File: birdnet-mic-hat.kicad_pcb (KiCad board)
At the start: 4 copper layers, 17.8 x 22.7 mm, 26 parts, among them J1 PJ-327A0-SMT, J3 DF40HC(3.5)-30DS-0.4V(51), Q1 MMBT3904, U1 TLV320ADC5140, U2 TPS7A2033PDBVR

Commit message: Apply 2026-10-18 design-review fixes before relayout
Schematic: R3 becomes a 100k SHDNZ pull-down; add 4.7k I2C pull-ups
(R9/R10), a 33R PDM_CLK series resistor (R11), and ESD9B5.0ST5G TVS
diodes on JACK_TIP/JACK_RING (D1/D2). C11 footprint unchanged (0603).

PCB: R11 at U1 pin 11, pull-ups and TVS diodes placed and routed;
direct top-copper ground bar from U1 AVSS (pin 4) to the VREF/MICBIAS/
AREG caps; C9 moved beside U2; U1 EPAD paste removed (vias to be
plugged at fab); ENIG finish; edge via moved inboard; new references
hidden.

Checkpoint only: C11 is parked off-board and its MIC_RING_N connection
is unrouted. This state precedes a full relayout.

Co-Authored-By: Claude Opus 5.5 <noreply@anthropic.com>
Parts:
- added D1: ESD9B5.0ST5G, Diode_SMD:D_SOD-923, F.Cu at (117.0, 116.8)
- added D2: ESD9B5.0ST5G, Diode_SMD:D_SOD-923, F.Cu at (103.2, 107.9)
- added R10: 4.7k, Resistor_SMD:R_0402_1005Metric, F.Cu at (105.4, 128.3)
- added R11: 33, Resistor_SMD:R_0402_1005Metric, F.Cu at (107.6, 118.7)
- added R9: 4.7k, Resistor_SMD:R_0402_1005Metric, F.Cu at (106.5, 128.3)
- R3: value 10k -> 100k
- moved C11 14.5 mm to (122.0, 118.0)
- moved C9 1.90 mm to (115.3, 123.8), turned to 180 degrees
- moved C4 0.60 mm to (113.4, 122.4)
- moved C1 0.58 mm to (113.4, 123.4)
- moved C5 0.50 mm to (113.4, 121.3)
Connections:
- R3 pad 1: VCC_3V3 -> GND
- U1 pad 11: /PDM_CLK -> Net-(U1-IN3M_GPO3)
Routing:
- net GND: track 22.3 -> 25.9 mm, vias 16 -> 18
- net /PDM_CLK: track 17.1 -> 14.2 mm
- net /JACK_RING: track 12.6 -> 15.2 mm
- net Net-(U1-IN3M_GPO3): track 0.00 -> 2.00 mm
- net AVDD: track 32.5 -> 34.2 mm
- net /MIC_RING_N: track 7.28 -> 8.72 mm
- net /JACK_BIAS_SENSE: track 40.0 -> 38.8 mm
- net /I2C_SCL: track 9.19 -> 10.1 mm, vias 1 -> 2
- net /I2C_SDA: track 11.7 -> 12.5 mm, vias 1 -> 2
- net /JACK_TIP: track 11.2 -> 11.9 mm

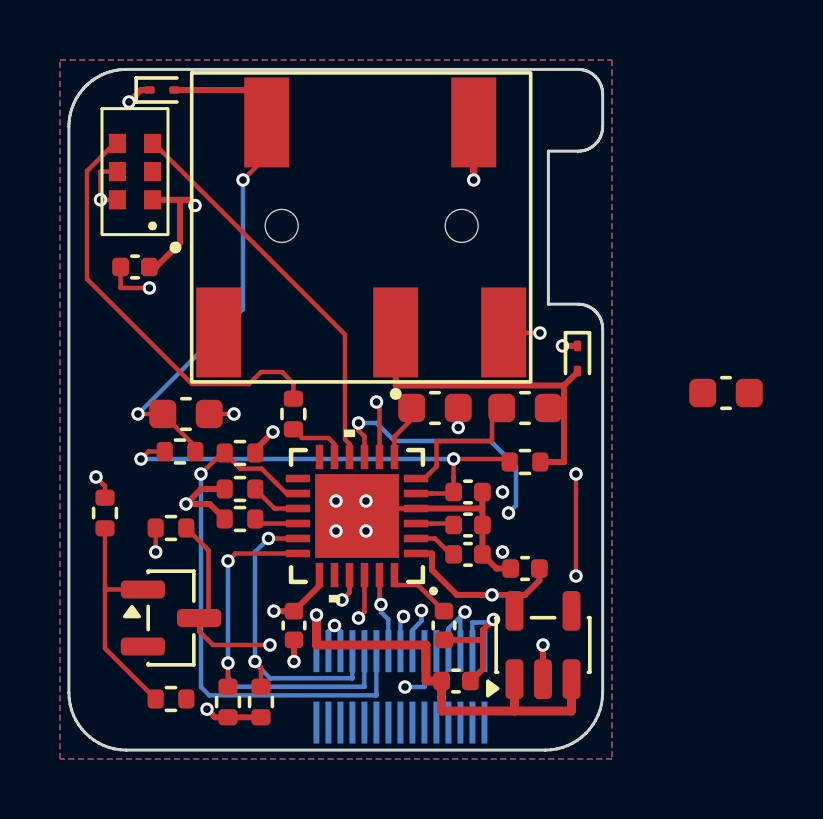
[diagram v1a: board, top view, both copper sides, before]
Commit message: Relayout: route board, swap J3 I2S/I2C GPIO assignment
Full re-route of the 2026-10-18 relayout. J3 signals were permuted so
I2S drops straight down from U1 pins 21-23: 8 SDOUT/GPIO42,
10 BCLK/GPIO41, 12 WS/GPIO40, 14 SCL/GPIO39, 16 SDA/GPIO38,
18 ADC_RST/GPIO47, 20 MIC_PRESENT/GPIO48. Firmware must follow.

U1 pad 4 zone connection set to solid (hard-wired AVSS bar).
DRC: 0 errors, 0 unconnected, parity 0; 2 known U1/J3 library
mismatch warnings. ERC: 0/0.

Co-Authored-By: Claude Opus 5.5 <noreply@anthropic.com>
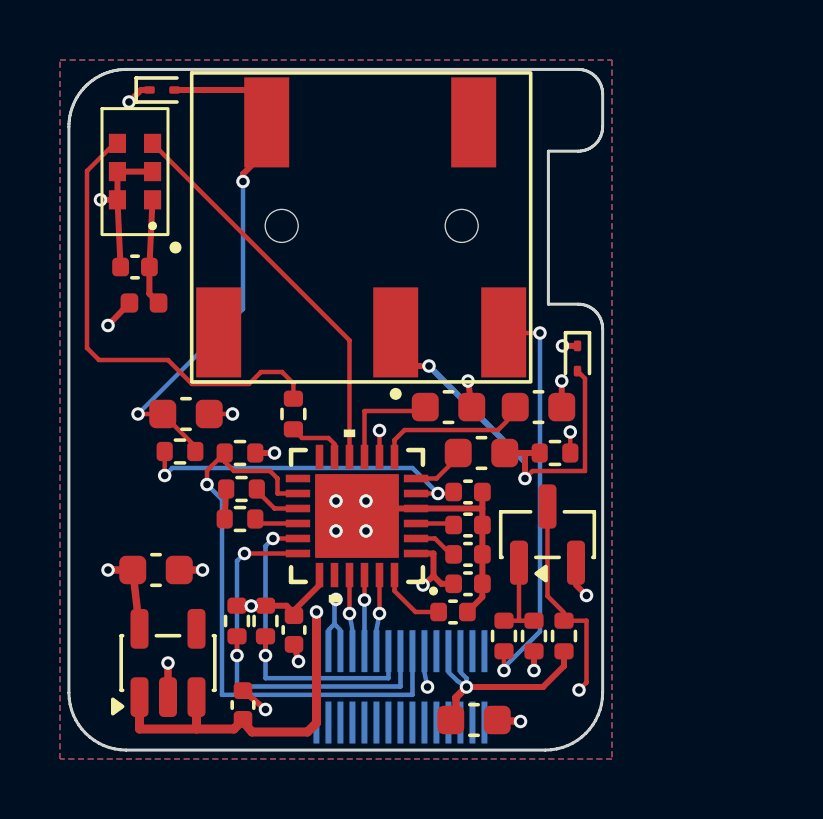
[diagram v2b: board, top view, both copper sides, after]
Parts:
- added C13: 10uF, Capacitor_SMD:C_0603_1608Metric, F.Cu at (103.0, 123.9)
- added C14: 10uF, Capacitor_SMD:C_0603_1608Metric, F.Cu at (113.6, 128.9)
- added FB1: 600R@100MHz, Inductor_SMD:L_0402_1005Metric, F.Cu at (102.6, 115.0)
- moved R6 13.9 mm to (114.6, 126.1), turned to 90 degrees
- moved R7 13.6 mm to (116.6, 126.1), turned to 90 degrees
- moved Q1 12.9 mm to (116.0, 122.7), turned to 90 degrees
- moved U2 12.5 mm to (103.4, 127.0)
- moved R8 12.3 mm to (115.6, 126.1), turned to -90 degrees
- moved C11 9.26 mm to (112.8, 118.5), turned to 0 degrees
- moved C8 7.14 mm to (105.9, 128.4), turned to 90 degrees
- moved C10 3.45 mm to (115.8, 118.5)
- moved R10 2.72 mm to (105.7, 125.6), turned to -90 degrees
- moved R9 2.70 mm to (106.7, 125.6), turned to -90 degrees
- moved C2 2.09 mm to (113.8, 120.0)
- moved C9 1.97 mm to (113.4, 124.4), turned to 0 degrees
- moved R1 1.04 mm to (116.3, 120.0), turned to 180 degrees
- moved C6 0.54 mm to (112.9, 125.3), turned to 0 degrees
- moved C7 0.15 mm to (107.6, 125.9)
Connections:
- C12 pad 1: AVDD -> MIC_VDD
- J3 pad 10: /I2C_SDA -> /I2S_BCLK
- J3 pad 12: /ADC_RST -> /I2S_WS
- J3 pad 14: /I2S_WS -> /I2C_SCL
- J3 pad 16: /I2S_SDOUT -> /I2C_SDA
- J3 pad 18: /I2S_BCLK -> /ADC_RST
- J3 pad 8: /I2C_SCL -> /I2S_SDOUT
- MK1 pad 1: AVDD -> MIC_VDD
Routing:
- net /JACK_BIAS_SENSE: track 38.8 -> 13.0 mm, vias 4 -> 2
- net AVDD: track 34.2 -> 25.5 mm, vias 2 -> 3
- net /MIC_RING_N: track 8.72 -> 3.18 mm, vias 2 -> 0
- net Net-(Q1-B): track 7.65 -> 2.19 mm
- net VCC_3V3: track 23.2 -> 18.4 mm, vias 4 -> 2
- net /I2S_BCLK: track 5.79 -> 1.84 mm, vias 2 -> 1
- net MIC_VDD: track 0.00 -> 3.57 mm
- net /MIC_TIP: track 4.98 -> 1.52 mm
- net /I2S_SDOUT: track 4.82 -> 1.85 mm, vias 2 -> 1
- net /MIC_TIP_N: track 1.87 -> 4.57 mm
- net MICBIAS: track 15.8 -> 18.2 mm, vias 2 -> 3
- net GND: track 25.9 -> 23.6 mm
- net VIN: track 14.7 -> 12.7 mm
- net /MIC_PRESENT: track 13.5 -> 12.1 mm
- net /PDM_CLK: track 14.2 -> 15.5 mm
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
